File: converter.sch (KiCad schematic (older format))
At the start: 49 parts, among them J1 A04, J10 B08, J11 A02, J12 A03, J13 A04, J2 B08, J3 A01, J4 A02, J5 A03, J6 TEENSY INTERNAL PINS, J7 Screw_Terminal_01x02, J8 BLUEFRUIT LE SPI FRIEND, J9 A01, K1 DIP05-1C90-51D, SW1 PROG SEL, SW10 MC, SW11 AUX DUP, SW12 BAIL 8, SW13 PROG 1, SW14 LATCH 30, SW15 REL, SW16 RESTORE BAIL CONTACT, SW17 FEED, SW18 REGISTER LATCH, SW19 PROG 2, SW2 AUTO DUP, SW20 DUP, SW21 MULTI PCH (OUTBOUND), SW22 ALPHA, SW23 NUMERIC, SW24 MULTI PCH (INBOARD), SW25 SPACE LATCH, SW26 ERROR RESET, SW27 BAIL 9, SW3 CLEAR, SW4 PRINT, SW5 LZ PRINT, SW6 INTERPRET PUNCH, SW7 AUTO FEED, SW8 SKIP, SW9 LEFT ZERO, U1 SSTW003A0A41Z, U2 Teensy++2.0

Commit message: various varigations verified vicariously, verily verbose
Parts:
- SW16: value RESTORE BAIL CONTACT -> (NC) RESTORE BAIL CONTACT
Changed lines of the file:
@@
 Wire Wire Line
 	2950 9740 3460 9740
-Text Label 2950 9750 0    60   ~ 0
+Text Label 2950 9740 0    60   ~ 0
 +VOUT
 Text Label 2950 9840 0    60   ~ 0
@@
 P 4290 4120
 F 0 "SW16" H 4290 4245 50  0000 C CNN
-F 1 "RESTORE BAIL CONTACT" H 4290 4020 50  0000 L CNN
+F 1 "(NC) RESTORE BAIL CONTACT" H 4030 4030 50  0000 L CNN
 F 2 "" H 4290 4120 50  0001 C CNN
 F 3 "" H 4290 4120 50  0001 C CNN

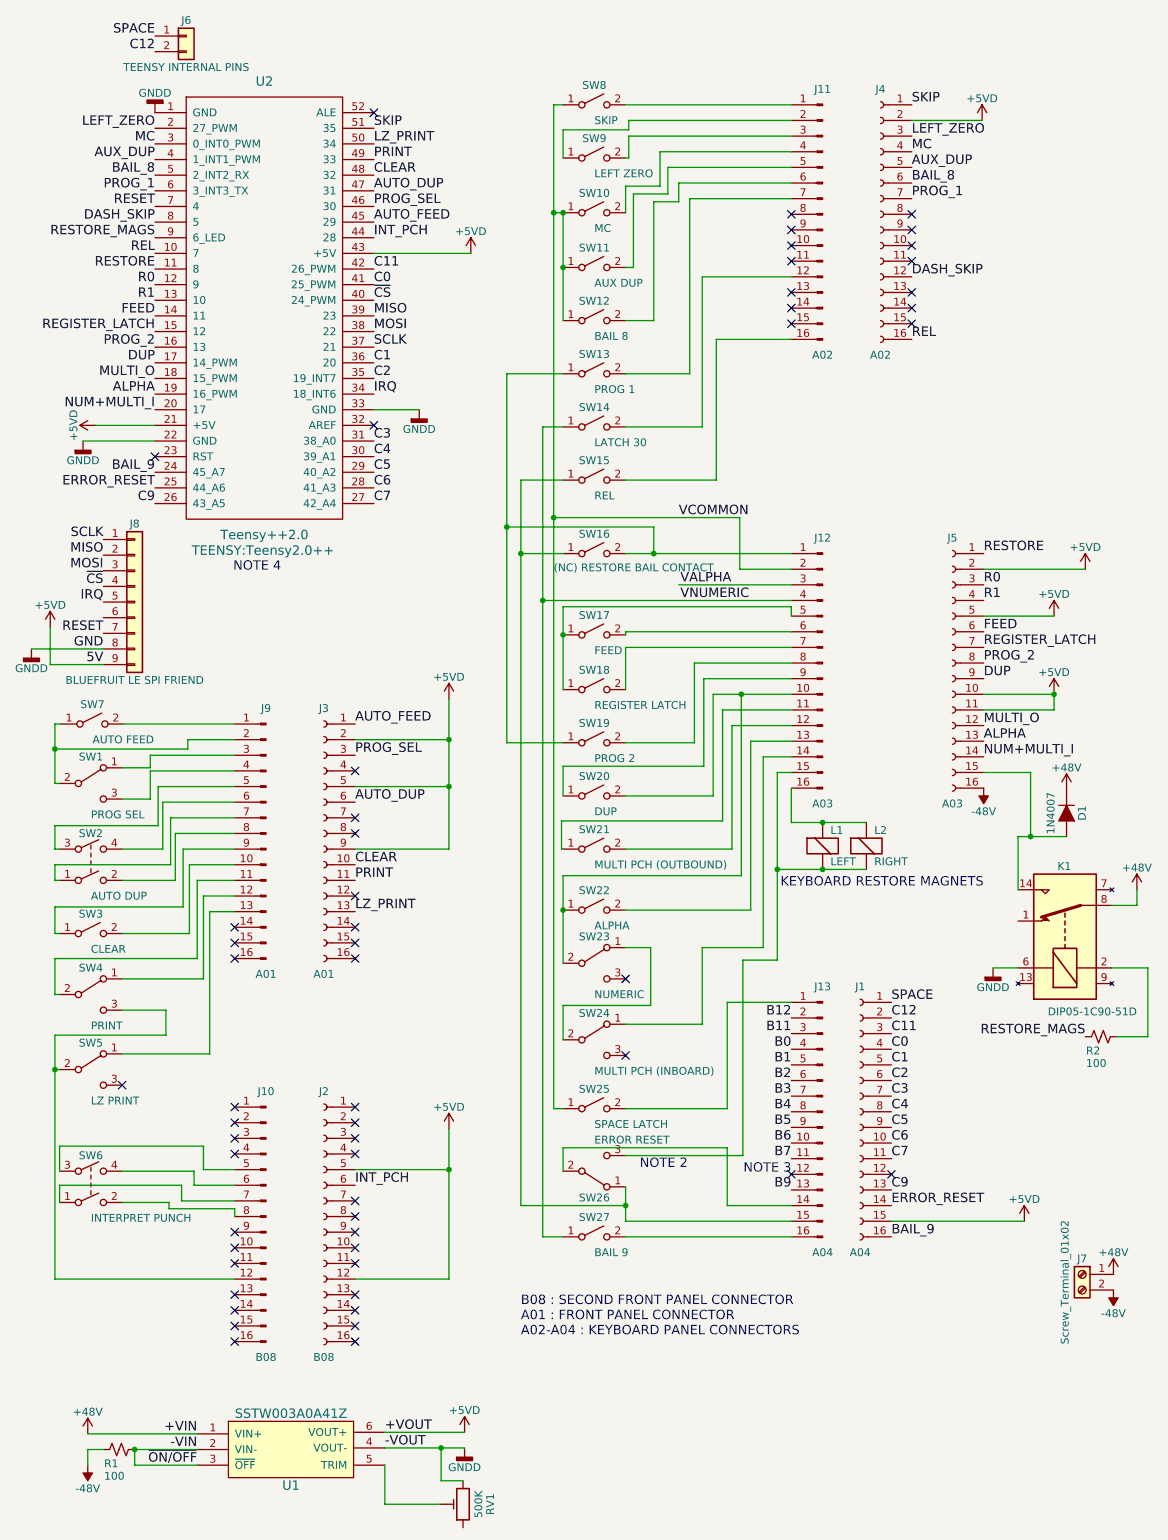
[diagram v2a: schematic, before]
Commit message: updated flyback diode footprint, and cleaned up some of the silkscreening
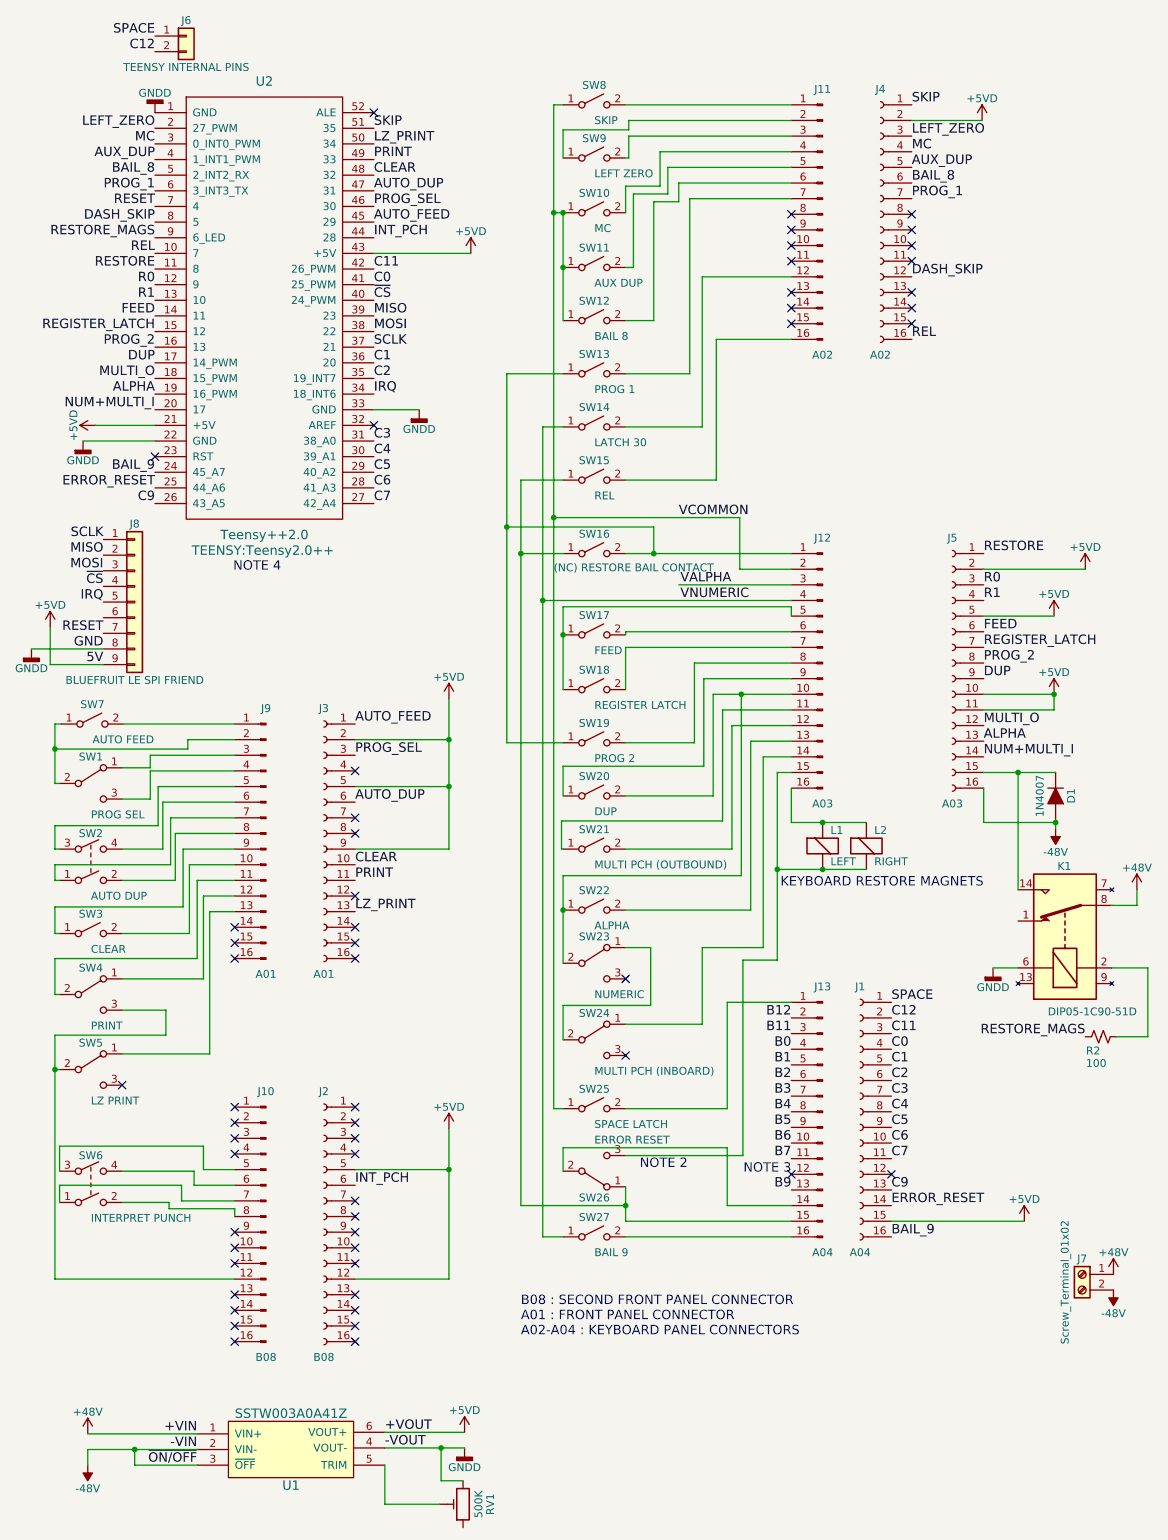
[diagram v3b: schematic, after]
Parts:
- removed R1: 100, Resistors_THT:R_Axial_DIN0204_L3.6mm_D1.6mm_P5.08mm_Vertical, symbol Device:R_Small_US
- D1: footprint Diodes_THT:D_T-1_P2.54mm_Vertical_AnodeUp -> Diode_THT:D_T-1_P10.16mm_Horizontal
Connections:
- net -VIN is gone; now on net -48V: U1.2 (VIN-), U1.3 (~OFF)
- net +48V: no longer D1.1 (K)
- net -48V: now also D1.2 (A)
- net at J5.15 (Pin_15), K1.14: now also D1.1 (K); no longer D1.2 (A)
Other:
- moved on the sheet: D1
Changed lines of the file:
@@
 L Device:D_ALT D1
 U 1 1 5C16B8FA
-P 7310 5780
-F 0 "D1" H 7310 5880 50  0000 C CNN
-F 1 "1N4007" H 7310 5680 50  0000 C CNN
-F 2 "Diodes_THT:D_T-1_P2.54mm_Vertical_AnodeUp" H 7310 5780 50  0001 C CNN
-F 3 "" H 7310 5780 50  0001 C CNN
-	1    7310 5780
+P 7240 5670
+F 0 "D1" H 7240 5770 50  0000 C CNN
+F 1 "1N4007" H 7240 5570 50  0000 C CNN
+F 2 "Diode_THT:D_T-1_P10.16mm_Horizontal" H 7240 5670 50  0001 C CNN
+F 3 "" H 7240 5670 50  0001 C CNN
+	1    7240 5670
 	0    1    1    0
 $EndComp
@@
 	7000 6770 6840 6770
 Wire Wire Line
-	7080 5930 7080 5520
-Wire Wire Line
-	7080 5520 6780 5520
+	7000 5520 6780 5520
 $Comp
 L sstw003a0a41z:SSTW003A0A41Z U1
@@
 Wire Wire Line
 	1020 3400 1480 3400
-Wire Wire Line
-	7000 5930 7080 5930
-$Comp
-L power:+48V #PWR018
-U 1 1 5CB26CBF
-P 7310 5630
-F 0 "#PWR018" H 7310 5480 50  0001 C CNN
-F 1 "+48V" H 7310 5770 50  0000 C CNN
-F 2 "" H 7310 5630 50  0001 C CNN
-F 3 "" H 7310 5630 50  0001 C CNN
-	1    7310 5630
-	-1   0    0    -1
-$EndComp
-Wire Wire Line
-	7000 6270 7000 5930
-Connection ~ 7080 5930
 NoConn ~ 2880 1300
 NoConn ~ 1480 3500
@@
 L power:-48V #PWR0105
 U 1 1 5CB40424
-P 6780 5620
-F 0 "#PWR0105" H 6780 5720 50  0001 C CNN
-F 1 "-48V" H 6780 5770 50  0000 C CNN
-F 2 "" H 6780 5620 50  0001 C CNN
-F 3 "" H 6780 5620 50  0001 C CNN
-	1    6780 5620
+P 7240 5880
+F 0 "#PWR0105" H 7240 5980 50  0001 C CNN
+F 1 "-48V" H 7240 6030 50  0000 C CNN
+F 2 "" H 7240 5880 50  0001 C CNN
+F 3 "" H 7240 5880 50  0001 C CNN
+	1    7240 5880
 	-1   0    0    1
 $EndComp
@@
 Wire Wire Line
 	1350 9950 1750 9950
-Wire Wire Line
-	7080 5930 7310 5930
 $Comp
 L power:+48V #PWR0102
@@
 Wire Wire Line
 	1350 9950 1350 9850
-$Comp
-L Device:R_Small_US R1
-U 1 1 5D248653
-P 1250 9850
-F 0 "R1" V 1340 9800 50  0000 C CNN
-F 1 "100" V 1420 9820 50  0000 C CNN
-F 2 "Resistors_THT:R_Axial_DIN0204_L3.6mm_D1.6mm_P5.08mm_Vertical" H 1250 9850 50  0001 C CNN
-F 3 "~" H 1250 9850 50  0001 C CNN
-	1    1250 9850
-	0    1    1    0
-$EndComp
-Connection ~ 1350 9850
 Wire Wire Line
 	1050 9750 1750 9750
 Wire Wire Line
-	1150 9850 1050 9850
+	1350 9850 1050 9850
 Wire Wire Line
 	1050 9850 1050 9950
@@
 Wire Wire Line
 	3310 9840 3460 9840
+Wire Wire Line
+	7000 5520 7000 6270
+Wire Wire Line
+	7240 5820 7240 5840
+Wire Wire Line
+	7240 5520 7000 5520
+Connection ~ 7000 5520
+Wire Wire Line
+	6780 5620 6780 5840
+Wire Wire Line
+	6780 5840 7240 5840
+Connection ~ 7240 5840
+Wire Wire Line
+	7240 5840 7240 5880
+Connection ~ 1350 9850
 $EndSCHEMATC
